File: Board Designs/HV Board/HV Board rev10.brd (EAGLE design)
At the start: 118.6 x 71.4 mm, 62 parts, among them IC1 OKI-78SR-5, IC2 NE5532SOIC

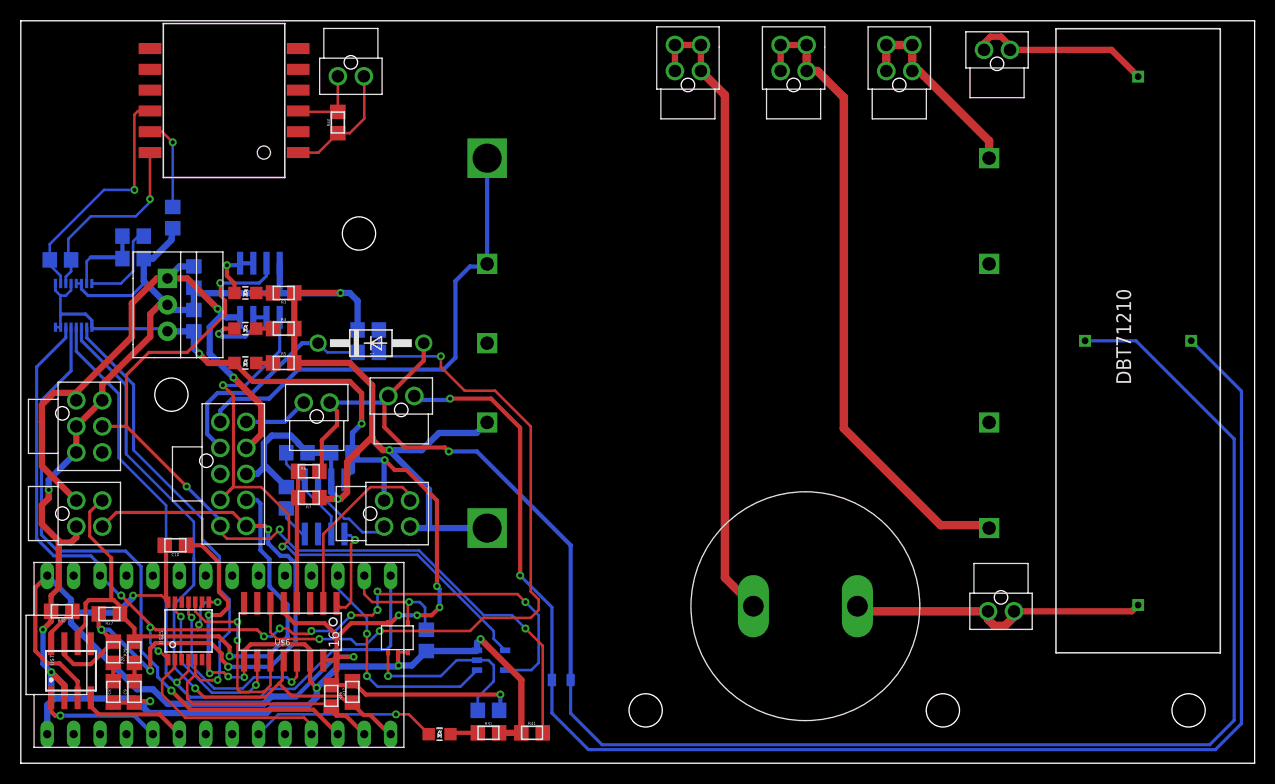
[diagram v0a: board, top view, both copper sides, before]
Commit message: HV board rev10: moved LTC6820 and screw
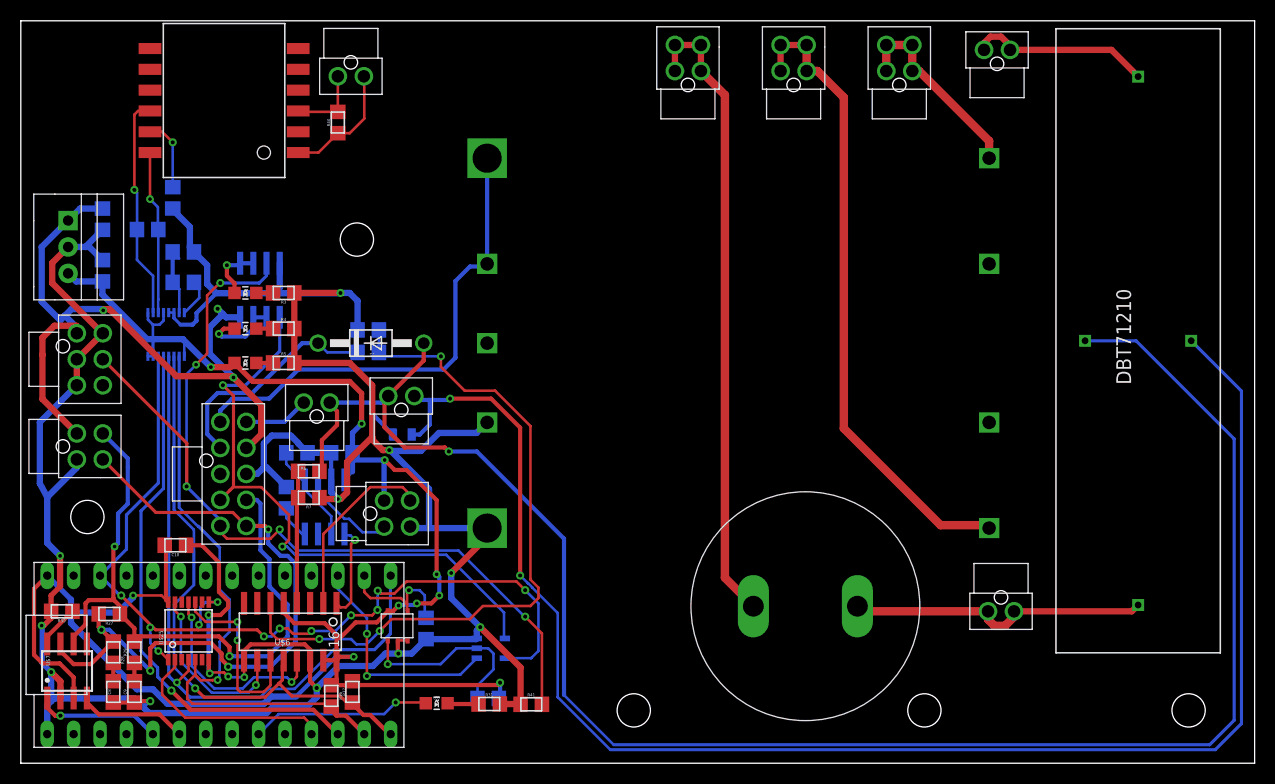
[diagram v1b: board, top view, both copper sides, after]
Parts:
- D2: value DIODE0805 -> TS4148 RYG
- moved D2 28.1 mm to (36.7, 31.6), turned to 0 degrees
- moved IC1 11.1 mm to (4.55, 49.6)
- moved C2 10.4 mm to (7.85, 52.3)
- moved C3 10.0 mm to (7.85, 47.3)
- moved U$8 9.32 mm to (15.6, 39.6)
- moved R35 8.88 mm to (12.2, 51.3)
- moved R33 6.56 mm to (15.6, 46.2)
- moved IMD 6.45 mm to (5.38, 38.8)
- moved POWER 6.45 mm to (5.38, 30.5)
- moved R34 4.87 mm to (15.6, 49.1)
- moved LED 2.98 mm to (40.0, 5.77)
- moved R31 2.77 mm to (45.0, 5.69)
- moved R41 2.74 mm to (49.1, 5.66)
- moved C4 1.91 mm to (14.6, 54.4)
- moved R42 1.14 mm to (39.0, 13.0)
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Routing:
- net GND: track 282.5 -> 298.6 mm, vias 14 -> 15
- net +12V: track 58.0 -> 70.9 mm, vias 2 -> 3
- net CS_LTC6820: track 62.9 -> 52.0 mm
- net SCK_TEENSY: track 71.1 -> 63.9 mm
- net CANL: track 55.6 -> 62.5 mm, vias 1 -> 2
- net MISO: track 65.1 -> 58.6 mm
- net MOSI_TEENSY: track 65.2 -> 58.8 mm
- net +5V: track 186.2 -> 192.2 mm
- net +3V3: track 95.6 -> 89.9 mm
- net N$31: track 8.56 -> 4.24 mm
- net OKHS: track 87.1 -> 91.0 mm, vias 4 -> 5
- net DISCHARGE_RELAY_GND: track 147.8 -> 151.2 mm
- net SHUTDOWN7: track 173.2 -> 176.5 mm
- net IP: track 18.7 -> 15.7 mm
- net IM: track 23.4 -> 21.4 mm
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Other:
- board text added: "2019 HV_board_rev10 Designed by Yvonne Yeh"
- board text added: "C:/Users/yyeh8/Documents/GitHub/circuits-2019/EAGLE Supporting Files/Bitmaps for logos/HyTech_square.bmp"
- board text removed: "2019_hv_board_rev10"
- board text removed: "Designed by Yvonne Yeh"

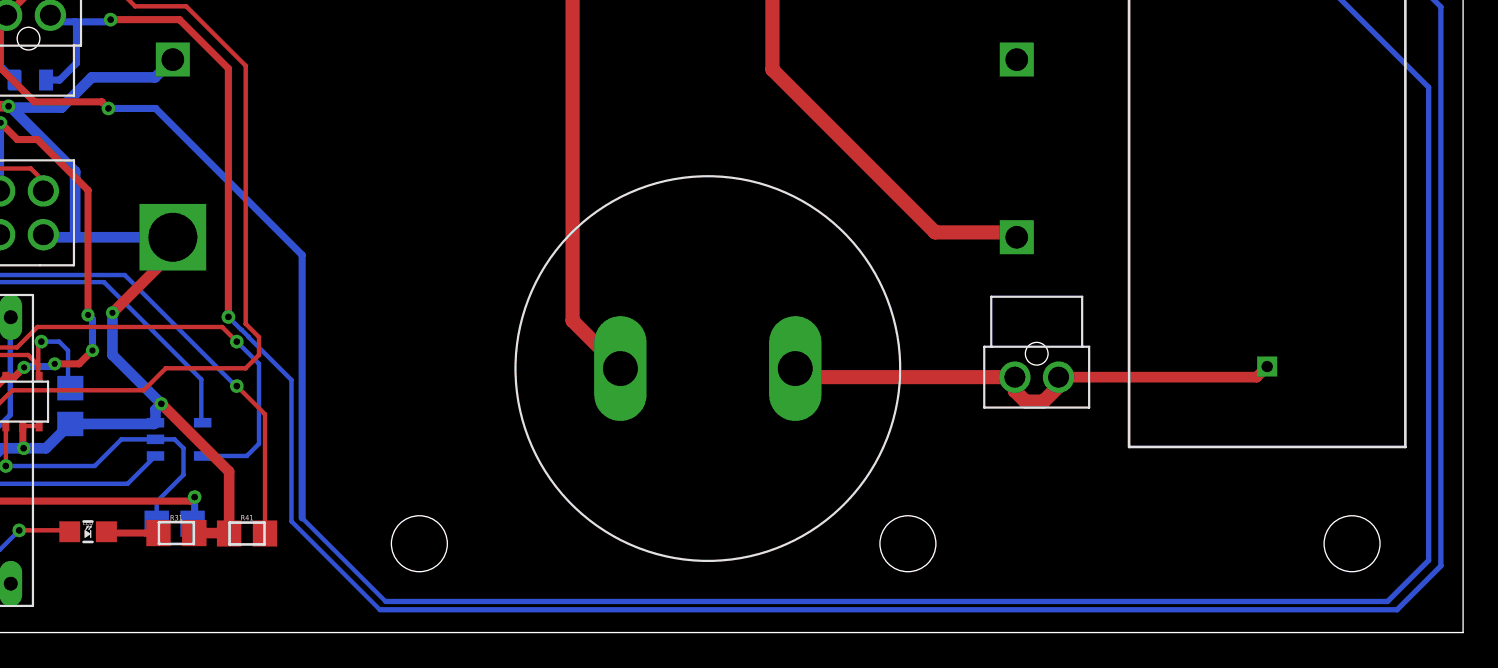
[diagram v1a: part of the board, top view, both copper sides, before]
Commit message: BMS segment rev9: moved resistors, modified silkscreen
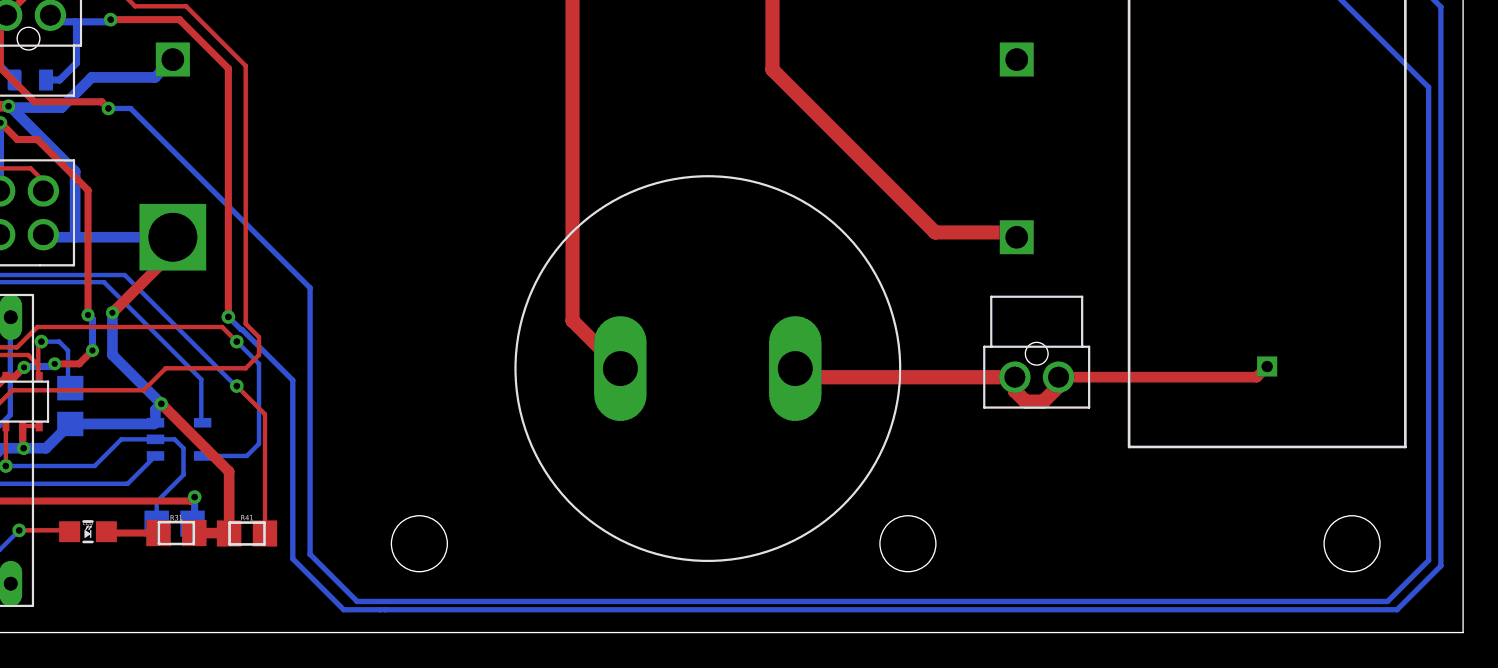
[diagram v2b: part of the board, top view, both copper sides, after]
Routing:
- net DISCHARGE_RELAY_GND: track 151.2 -> 152.4 mm
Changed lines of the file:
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@@
 <wire x1="116.6474" y1="31.1806" x2="116.6474" y2="4.1254" width="0.3048" layer="16"/>
 <wire x1="116.6474" y1="4.1254" x2="114.3" y2="1.778" width="0.3048" layer="16"/>
-<wire x1="114.3" y1="1.778" x2="56.9976" y2="1.778" width="0.3048" layer="16"/>
+<wire x1="114.3" y1="1.778" x2="55.372" y2="1.778" width="0.3048" layer="16"/>
 <wire x1="38.735" y1="38.715" x2="35.326" y2="35.306" width="0.4064" layer="1"/>
 <wire x1="38.735" y1="40.386" x2="38.735" y2="38.715" width="0.4064" layer="1"/>
@@
 <wire x1="34.691" y1="34.671" x2="33.7312" y2="34.671" width="0.4064" layer="16"/>
 <wire x1="33.7312" y1="34.671" x2="29.698" y2="34.671" width="0.4064" layer="16"/>
-<wire x1="43.842" y1="29.972" x2="52.224" y2="21.59" width="0.4064" layer="16"/>
-<wire x1="43.842" y1="29.972" x2="41.148" y2="29.972" width="0.4064" layer="16"/>
 <contactref element="R6" pad="1"/>
 <wire x1="28.941984375" y1="31.054534375" x2="28.941984375" y2="28.297984375" width="0.4064" layer="1"/>
@@
 <wire x1="35.7776" y1="31.5976" x2="33.7312" y2="33.644" width="0.4064" layer="16"/>
 <wire x1="33.7312" y1="33.644" x2="33.7312" y2="34.671" width="0.4064" layer="16"/>
-<wire x1="52.224" y1="6.5516" x2="52.224" y2="21.59" width="0.4064" layer="16"/>
-<wire x1="56.9976" y1="1.778" x2="52.224" y2="6.5516" width="0.254" layer="16"/>
+<wire x1="55.372" y1="1.778" x2="52.6796" y2="4.4704" width="0.3048" layer="16"/>
+<wire x1="52.6796" y1="19.7104" x2="52.6796" y2="4.4704" width="0.3048" layer="16"/>
+<wire x1="41.148" y1="29.972" x2="42.418" y2="29.972" width="0.3048" layer="16"/>
+<wire x1="42.418" y1="29.972" x2="52.6796" y2="19.7104" width="0.3048" layer="16"/>
 </signal>
 <signal name="SHUTDOWN6">
@@
 <contactref element="U$4" pad="COIL-"/>
 <wire x1="112.516" y1="40.612" x2="117.348" y2="35.78" width="0.3048" layer="16"/>
-<wire x1="114.842628125" y1="1.304628125" x2="56.6674" y2="1.304628125" width="0.3048" layer="16"/>
+<wire x1="114.842628125" y1="1.304628125" x2="56.9722" y2="1.304628125" width="0.3048" layer="16"/>
+<wire x1="56.9722" y1="1.304628125" x2="56.6674" y2="1.304628125" width="0.3048" layer="16"/>
 <wire x1="117.348" y1="3.81" x2="114.842628125" y2="1.304628125" width="0.3048" layer="16"/>
 <wire x1="117.348" y1="35.78" x2="117.348" y2="3.81" width="0.3048" layer="16"/>
@@
 <wire x1="39.3192" y1="32.5628" x2="39.3192" y2="34.8234" width="0.4064" layer="16"/>
 <wire x1="39.3192" y1="34.8234" x2="39.2176" y2="34.925" width="0.4064" layer="16"/>
-<wire x1="51.6128" y1="6.359228125" x2="56.6674" y2="1.304628125" width="0.254" layer="16"/>
-<wire x1="49.1617" y1="16.9158125" x2="49.1617" y2="16.8943" width="0.254" layer="16"/>
-<wire x1="48.7674125" y1="17.3101" x2="49.1617" y2="16.9158125" width="0.254" layer="16"/>
-<wire x1="48.006" y1="18.05" x2="48.7459" y2="17.3101" width="0.254" layer="16"/>
-<wire x1="48.7459" y1="17.3101" x2="48.7674125" y2="17.3101" width="0.254" layer="16"/>
-<wire x1="49.1617" y1="16.8943" x2="51.6128" y2="14.4432" width="0.254" layer="16"/>
-<wire x1="51.6128" y1="14.4432" x2="51.6128" y2="6.359228125" width="0.254" layer="16"/>
+<wire x1="48.006" y1="18.05" x2="48.7205" y2="17.3355" width="0.3048" layer="16"/>
+<wire x1="48.7205" y1="17.3355" x2="48.77793125" y2="17.3355" width="0.3048" layer="16"/>
+<wire x1="48.77793125" y1="17.3355" x2="51.689" y2="14.42443125" width="0.3048" layer="16"/>
+<wire x1="51.689" y1="14.42443125" x2="51.689" y2="4.2164" width="0.3048" layer="16"/>
+<wire x1="51.689" y1="4.2164" x2="54.600771875" y2="1.304628125" width="0.3048" layer="16"/>
+<wire x1="54.600771875" y1="1.304628125" x2="56.6674" y2="1.304628125" width="0.3048" layer="16"/>
 </signal>
 <signal name="N$24">

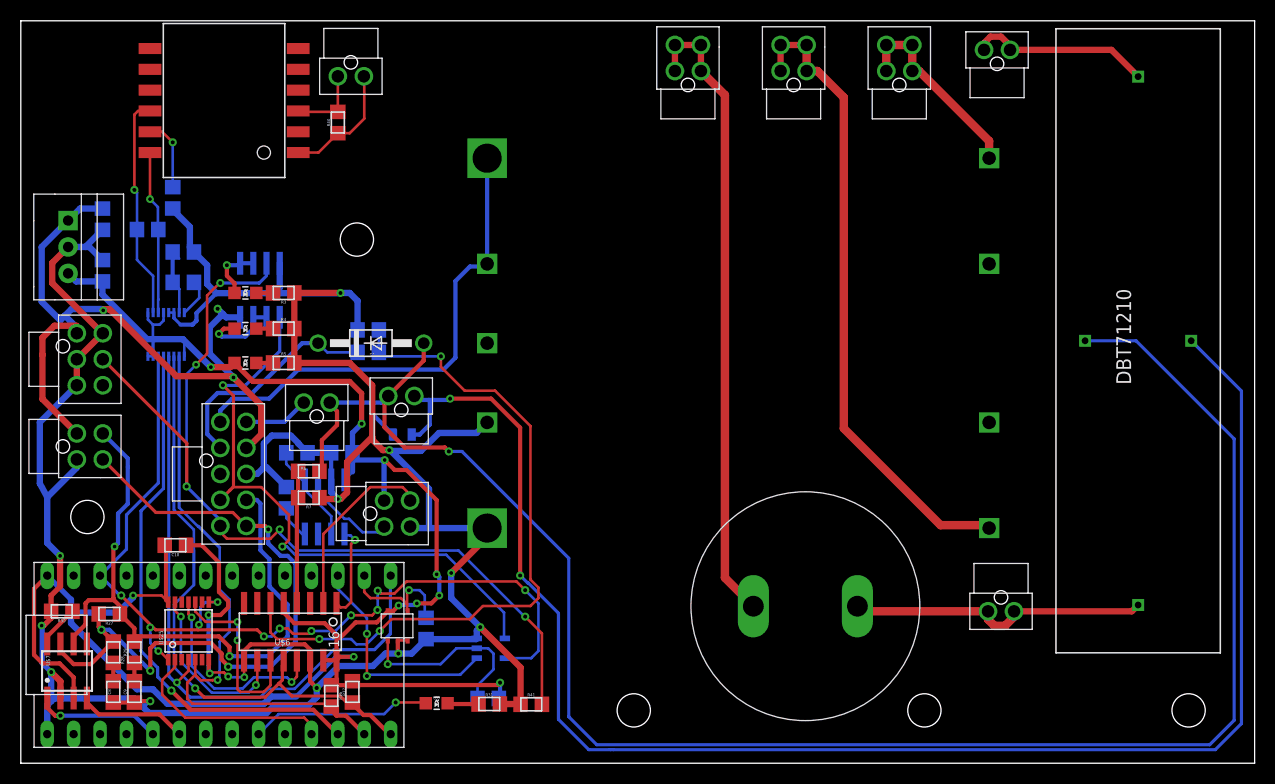
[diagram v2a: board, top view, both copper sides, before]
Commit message: BMS rev9, HV rev10: Small adjustments for manufacturing
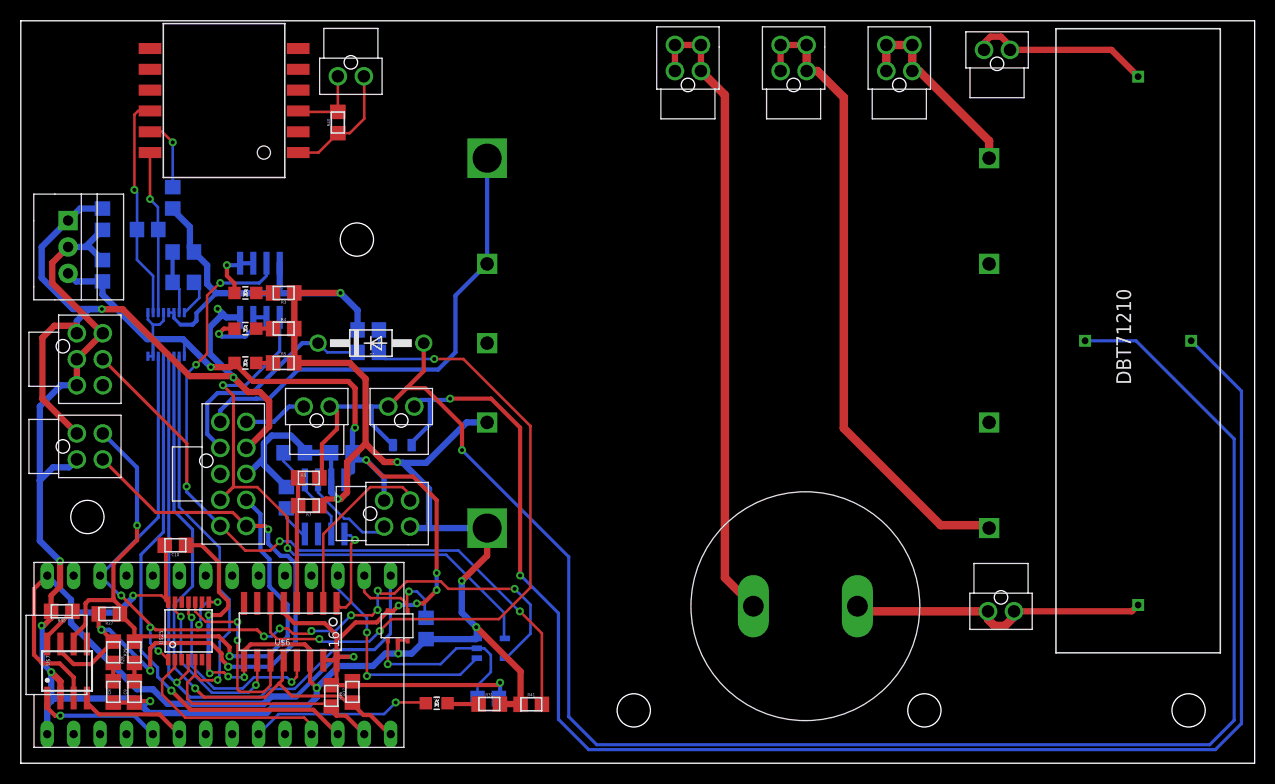
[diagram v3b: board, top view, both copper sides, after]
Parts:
- moved D2 1.02 mm to (36.7, 30.6)
- moved RELAYS 1.02 mm to (36.6, 34.3)
- moved R7 0.76 mm to (27.7, 24.8)
- moved R6 0.64 mm to (27.7, 27.4)
- moved INTERLOCK 0.38 mm to (28.4, 34.3)
- moved C6 0.25 mm to (26.3, 29.8)
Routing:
- net +5V: track 192.2 -> 189.1 mm
- net +3V3: track 89.9 -> 87.3 mm
- net N$24: track 68.0 -> 65.5 mm
- net GND: track 298.6 -> 296.9 mm
- net N$32: track 7.39 -> 6.14 mm
- net TSAL+: track 47.1 -> 45.9 mm
- net BMS_OK: track 58.7 -> 57.8 mm
- net +12V: track 70.9 -> 71.8 mm
- net DISCHARGE_RELAY_GND: track 152.4 -> 153.1 mm
- net N$9: track 12.7 -> 12.1 mm
- net N$50: track 12.4 -> 11.8 mm
- net OKHS: track 91.0 -> 90.4 mm
- net N$31: track 4.24 -> 3.72 mm
